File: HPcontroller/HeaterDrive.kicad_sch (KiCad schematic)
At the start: 10 parts, among them J1 Conn_01x02_Pin, U4 NCP81071B

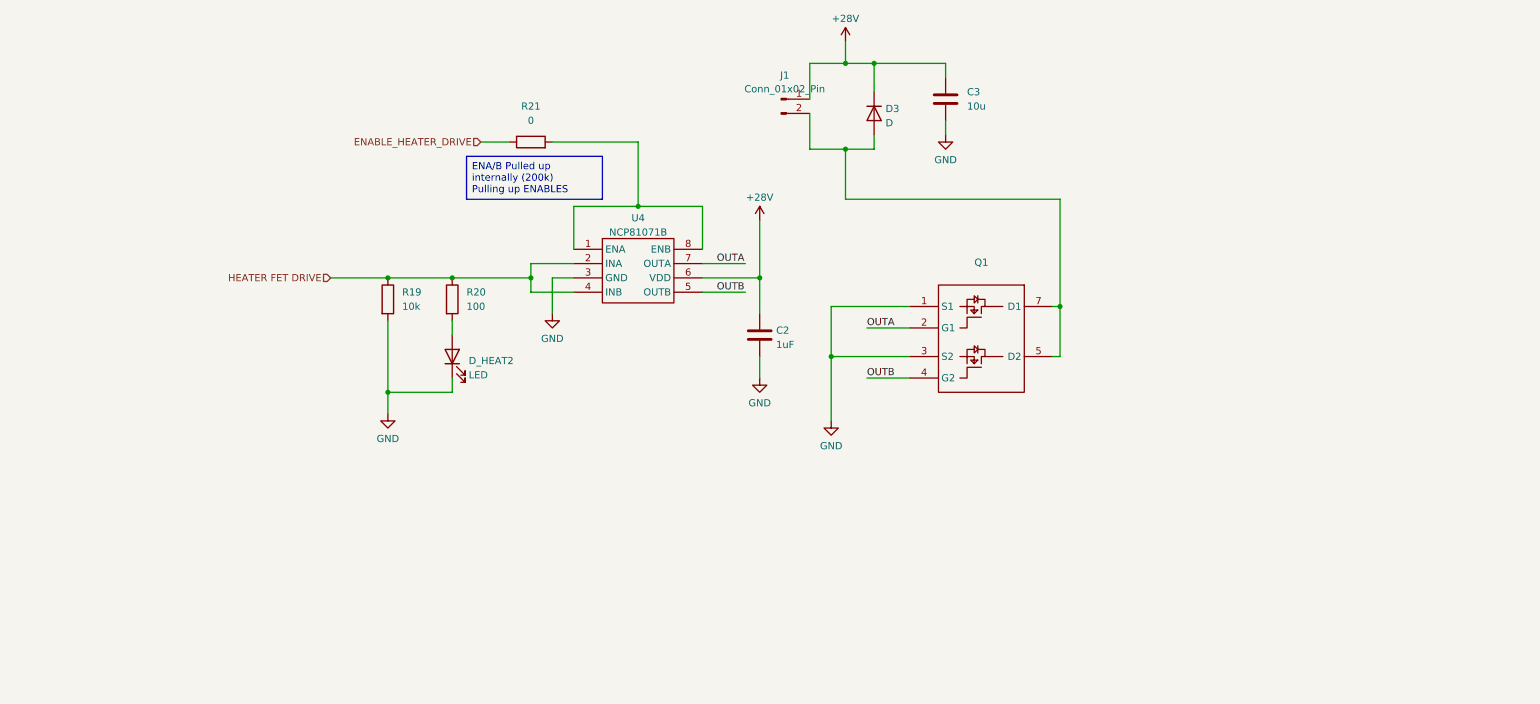
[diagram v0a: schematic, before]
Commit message: released rev c - op amp swap not fixed!
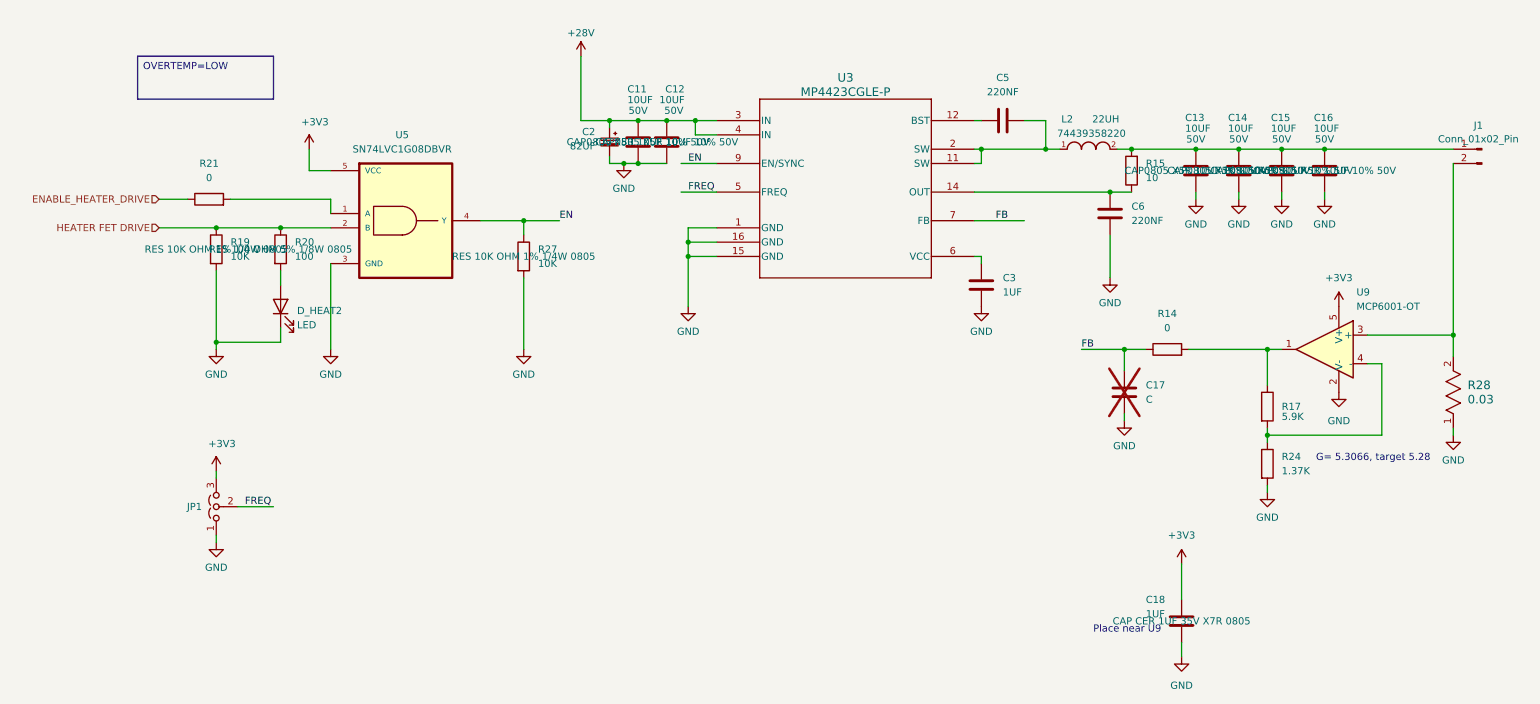
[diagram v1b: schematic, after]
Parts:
- removed C2: 1uF, Capacitor_SMD:C_0805_2012Metric, symbol Device:C
- removed D3: D, Diode_SMD:D_SMB_Handsoldering, symbol Device:D
- removed Q1: ~, hotplate_Library:LFPAK56D, symbol Hotplate_Library:BUK9K25-40RAX
- removed U4: NCP81071B, Package_SO:SOIC-8_3.9x4.9mm_P1.27mm, symbol project_assorted:NCP81071B
- added C11, C12, C13, C14, C15, C16: 10UF, Capacitor_SMD:C_0805_2012Metric, symbol Device:C
- added C17: C, Capacitor_SMD:C_0603_1608Metric, symbol Device:C
- added C18: 1UF, Capacitor_SMD:C_0805_2012Metric, symbol Device:C
- added C2: 82UF, Capacitor_SMD:CP_Elec_8x6.7, symbol Device:C_Polarized_Small
- added C5, C6: 220NF, Capacitor_SMD:C_0603_1608Metric, symbol Device:C
- added JP1: Jumper_3_Open, Jumper:SolderJumper-3_P1.3mm_Open_RoundedPad1.0x1.5mm, symbol Jumper:Jumper_3_Open
- added L2: 22UH, HPcontroller_kimera:WE-XHMI_8080, symbol HPcontroller_kimera:AMDLA1306S-220MT
- added R14: 0, Resistor_SMD:R_0805_2012Metric_Pad1.20x1.40mm_HandSolder, symbol Device:R
- added R15: 10, Resistor_SMD:R_0805_2012Metric_Pad1.20x1.40mm_HandSolder, symbol Device:R
- added R17: 5.9K, Resistor_SMD:R_0805_2012Metric_Pad1.20x1.40mm_HandSolder, symbol Device:R
- added R24: 1.37K, Resistor_SMD:R_0805_2012Metric_Pad1.20x1.40mm_HandSolder, symbol Device:R
- added R27: 10K, Resistor_SMD:R_0805_2012Metric_Pad1.20x1.40mm_HandSolder, symbol Device:R
- added R28: 0.03, HPcontroller_kimera:STA_CSSH2728_STP, symbol HPcontroller_kimera:CSSH2728FT30L0
- added U3: MP4423CGLE-P, HPcontroller_kimera:QFN-16_MPQ4423C_MNP, symbol HPcontroller_kimera:MP4423CGLE-P
- added U5: SN74LVC1G08DBVR, HPcontroller_kimera:SOT95P280X145-5N, symbol HPcontroller_kimera:SN74LVC1G08DBVR
- added U9: MCP6001-OT, Package_TO_SOT_SMD:SOT-23-5, symbol Amplifier_Operational:MCP6001-OT
- C3: value 10u -> 1UF; footprint Capacitor_SMD:C_0805_2012Metric -> Capacitor_SMD:C_0603_1608Metric; Digikey PN 490-18663-1-ND -> (none); MPN GRM21BR61H106KE43L -> CL10B105MO8NNWC; Manufacturer (none) -> Samsung Electro-Mechanics; Package (none) -> 0603; Supplier (none) -> DigiKey; Supplier_PN (none) -> 1276-6524-1-ND; Voltage 50V -> (none)
- R19: value 10k -> 10K; Manufacturer (none) -> Stackpole Electronics Inc; Package (none) -> 0805; Supplier (none) -> DigiKey; Supplier_PN (none) -> RNCP0805FTD10K0CT-ND
- R20: Manufacturer (none) -> TE Connectivity Passive Product; Package (none) -> 0805; Supplier (none) -> DigiKey; Supplier_PN (none) -> A130128CT-ND
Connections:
- net +28V: now also C11.1, C12.1, C2.1, U3.3 (IN), U3.4 (IN); no longer C3.1, J1.1 (Pin_1)
- net GND: now also C11.2, C12.2, C13.2, C14.2, C15.2, C16.2, C17.2, C18.2, C2.2, C6.1, JP1.1 (A), R24.2, R27.2, R28.1, U3.1 (GND), U3.15 (GND), U3.16 (GND), U5.3 (GND), U9.2 (V-)
- net HEATER FET DRIVE: now also U5.2 (B)
- net at J1.2 (Pin_2): now also R28.2, U9.3 (+)
- net at R21.2: now also U5.1 (A)
- new net: R14.2, R17.1, U9.1
- new net: C5.1, U3.12 (BST)
- new net: C5.2, L2.1, U3.11 (SW), U3.2 (SW)
- new net: U3.10 (NC), U3.13 (NC), U3.8 (NC)
- new net: C6.2, R15.1, U3.14 (OUT)
- new net: C3.1, U3.6 (VCC)
- new net: R17.2, R24.1, U9.4 (-)
- new net: C13.1, C14.1, C15.1, C16.1, J1.1 (Pin_1), L2.2, R15.2
- new net +3V3: C18.1, JP1.3 (B), U5.5 (VCC), U9.5 (V+)
- new net EN: R27.1, U3.9 (EN/SYNC), U5.4 (Y)
- new net FB: C17.1, R14.1, U3.7 (FB)
- new net FREQ: JP1.2 (C), U3.5 (FREQ)
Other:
- note added: "G= 5.3066, target 5.28"
- note added: "Place near U9"
- moved on the sheet: D_HEAT2, J1, R19, R20, R21
